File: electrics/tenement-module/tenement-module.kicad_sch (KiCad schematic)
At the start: 28 parts, among them J1 WMBus, J2 South, J3 West, J4 East, U1 BA033CC0FP-E2, U2 MCP23009-E_SS, U3 WIRL-WMB8, U4 MAX3486

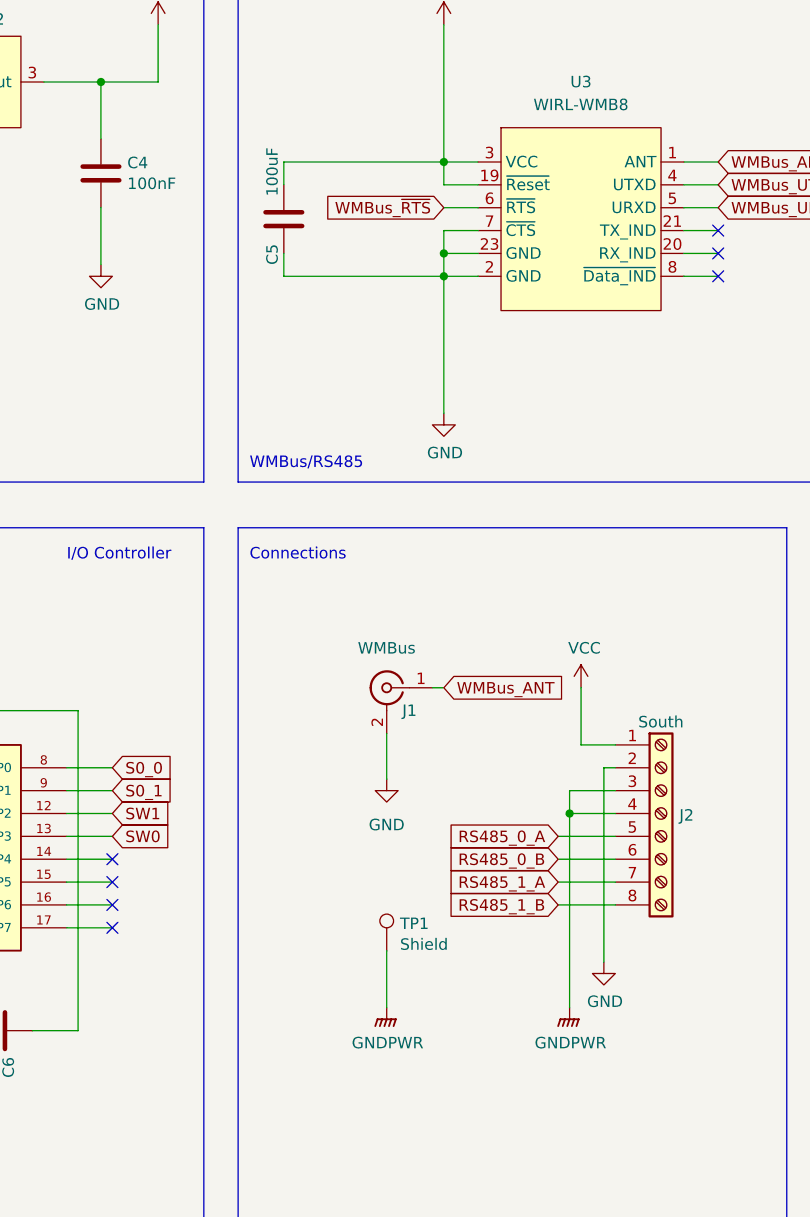
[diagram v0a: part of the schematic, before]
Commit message: Added product numbers for cost calculation
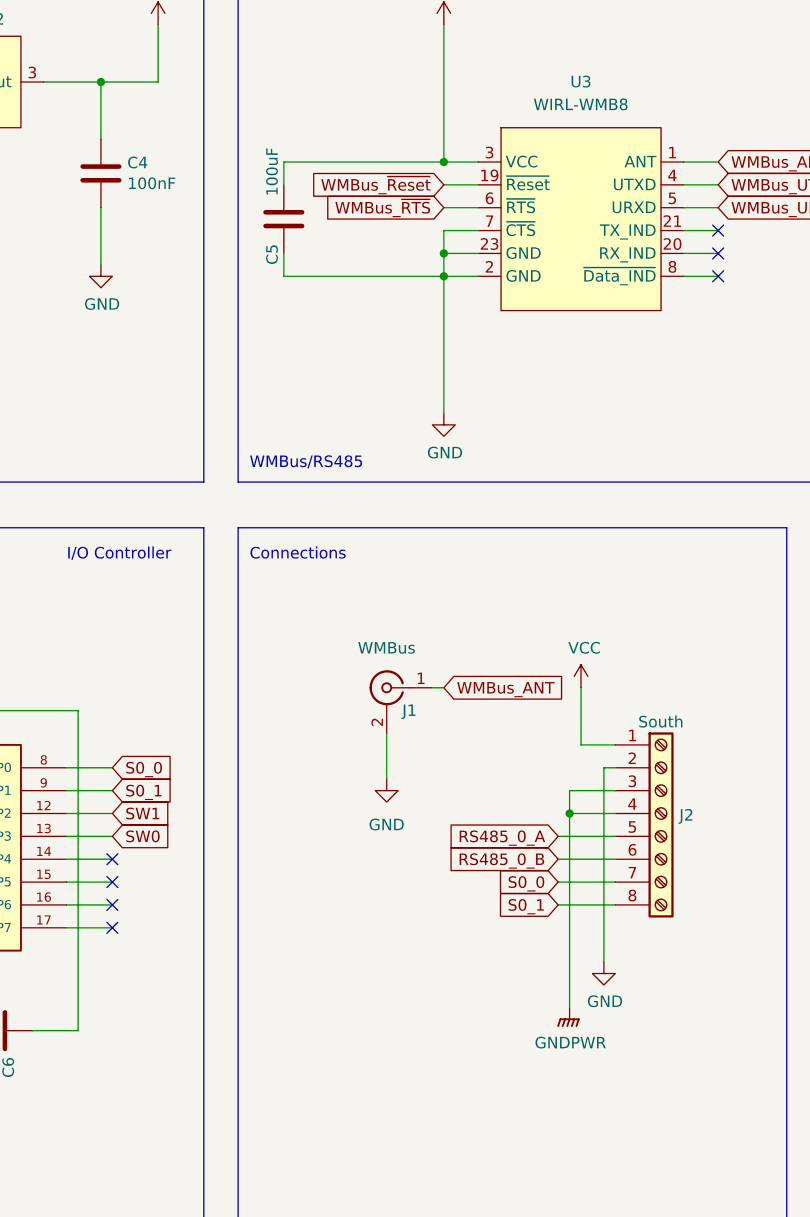
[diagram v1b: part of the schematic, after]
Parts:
- removed TP1: Shield, TestPoint:TestPoint_Pad_D4.0mm, symbol Connector:TestPoint
- J1: footprint (none) -> footprints:IPEX_20279-001E-01
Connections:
- net RS485_1_A is gone; now on net S0_0: J2.7 (Pin_7)
- net RS485_1_B is gone; now on net S0_1: J2.8 (Pin_8)
- net +3V3: no longer U3.19 (~{Reset})
- new net WMBus_~{Reset}: U3.19 (~{Reset})
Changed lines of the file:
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@@
   (junction (at 153.67 53.34) (diameter 0) (color 0 0 0 0)
   )
+  (junction (at 153.67 43.18) (diameter 0) (color 0 0 0 0)
+  )
   (junction (at 44.45 147.32) (diameter 0) (color 0 0 0 0)
   )
@@
   )
   (junction (at 153.67 55.88) (diameter 0) (color 0 0 0 0)
-  )
-  (junction (at 153.67 43.18) (diameter 0) (color 0 0 0 0)
   )
   (no_connect (at 184.15 55.88))
@@
   (no_connect (at 215.9 120.65))
   (no_connect (at 251.46 113.03))
-  (wire (pts (xy 147.32 130.81) (xy 147.32 137.16))
-    (stroke (width 0) (type default) (color 0 0 0 0))
-  )
   (polyline (pts (xy 130.81 78.74) (xy 130.81 20.32))
     (stroke (width 0) (type default) (color 0 0 0 0))
@@
     (stroke (width 0) (type default) (color 0 0 0 0))
   )
-  (wire (pts (xy 153.67 45.72) (xy 153.67 43.18))
-    (stroke (width 0) (type default) (color 0 0 0 0))
-  )
   (wire (pts (xy 157.48 53.34) (xy 153.67 53.34))
     (stroke (width 0) (type default) (color 0 0 0 0))
@@
     (stroke (width 0) (type default) (color 0 0 0 0))
   )
+  (wire (pts (xy 153.67 45.72) (xy 157.48 45.72))
+    (stroke (width 0) (type default) (color 0 0 0 0))
+  )
   (wire (pts (xy 153.67 55.88) (xy 157.48 55.88))
     (stroke (width 0) (type default) (color 0 0 0 0))
   )
-  (wire (pts (xy 157.48 45.72) (xy 153.67 45.72))
-    (stroke (width 0) (type default) (color 0 0 0 0))
-  )
   (wire (pts (xy 31.75 156.21) (xy 31.75 157.48))
     (stroke (width 0) (type default) (color 0 0 0 0))
@@
     (stroke (width 0) (type default) (color 0 0 0 0))
   )
+  (wire (pts (xy 153.67 43.18) (xy 157.48 43.18))
+    (stroke (width 0) (type default) (color 0 0 0 0))
+  )
   (wire (pts (xy 172.72 120.65) (xy 166.37 120.65))
     (stroke (width 0) (type default) (color 0 0 0 0))
@@
   )
   (wire (pts (xy 215.9 125.73) (xy 222.25 125.73))
-    (stroke (width 0) (type default) (color 0 0 0 0))
-  )
-  (wire (pts (xy 153.67 43.18) (xy 157.48 43.18))
     (stroke (width 0) (type default) (color 0 0 0 0))
   )
@@
     )
   )
+  (global_label "WMBus_~{Reset}" (shape input) (at 153.67 45.72 180) (fields_autoplaced)
+    (effects (font (size 1.27 1.27)) (justify right))
+    (property "Intersheet References" "${INTERSHEET_REFS}" (id 0) (at 138.8272 45.6406 0)
+      (effects (font (size 1.27 1.27)) (justify right) hide)
+    )
+  )
   (global_label "WMBus_UTXD" (shape input) (at 184.15 45.72 0) (fields_autoplaced)
     (effects (font (size 1.27 1.27)) (justify left))
@@
     )
   )
+  (global_label "S0_1" (shape input) (at 166.37 125.73 180) (fields_autoplaced)
+    (effects (font (size 1.27 1.27)) (justify right))
+    (property "Intersheet References" "${INTERSHEET_REFS}" (id 0) (at 279.4 259.08 0)
+      (effects (font (size 1.27 1.27)) hide)
+    )
+  )
   (global_label "WMBus_URXD" (shape input) (at 215.9 118.11 180) (fields_autoplaced)
     (effects (font (size 1.27 1.27)) (justify right))
@@
     (effects (font (size 1.27 1.27)) (justify right))
     (property "Intersheet References" "${INTERSHEET_REFS}" (id 0) (at 0 0 0)
+      (effects (font (size 1.27 1.27)) hide)
+    )
+  )
+  (global_label "S0_0" (shape input) (at 166.37 123.19 180) (fields_autoplaced)
+    (effects (font (size 1.27 1.27)) (justify right))
+    (property "Intersheet References" "${INTERSHEET_REFS}" (id 0) (at 279.4 210.82 0)
       (effects (font (size 1.27 1.27)) hide)
     )
@@
     )
   )
-  (global_label "RS485_1_A" (shape input) (at 166.37 123.19 180) (fields_autoplaced)
-    (effects (font (size 1.27 1.27)) (justify right))
-    (property "Intersheet References" "${INTERSHEET_REFS}" (id 0) (at -8.89 8.89 0)
-      (effects (font (size 1.27 1.27)) hide)
-    )
-  )
   (global_label "I2C_SDA" (shape input) (at 251.46 118.11 180) (fields_autoplaced)
     (effects (font (size 1.27 1.27)) (justify right))
@@
   )
   (global_label "RS485_0_A" (shape input) (at 166.37 118.11 180) (fields_autoplaced)
-    (effects (font (size 1.27 1.27)) (justify right))
-    (property "Intersheet References" "${INTERSHEET_REFS}" (id 0) (at -8.89 8.89 0)
-      (effects (font (size 1.27 1.27)) hide)
-    )
-  )
-  (global_label "RS485_1_B" (shape input) (at 166.37 125.73 180) (fields_autoplaced)
     (effects (font (size 1.27 1.27)) (justify right))
     (property "Intersheet References" "${INTERSHEET_REFS}" (id 0) (at -8.89 8.89 0)
@@
     (pin "1")
     (pin "2")
-  )
-  (symbol (lib_id "Connector:TestPoint") (at 147.32 130.81 0) (unit 1)
-    (in_bom yes) (on_board yes)
-    (property "Reference" "TP1" (id 0) (at 148.7932 127.8128 0)
-      (effects (font (size 1.27 1.27)) (justify left))
-    )
-    (property "Value" "Shield" (id 1) (at 148.7932 130.1242 0)
-      (effects (font (size 1.27 1.27)) (justify left))
-    )
-    (property "Footprint" "TestPoint:TestPoint_Pad_D4.0mm" (id 2) (at 152.4 130.81 0)
-      (effects (font (size 1.27 1.27)) hide)
-    )
-    (property "Datasheet" "~" (id 3) (at 152.4 130.81 0)
-      (effects (font (size 1.27 1.27)) hide)
-    )
-    (pin "1")
-  )
-  (symbol (lib_id "power:GNDPWR") (at 147.32 137.16 0) (unit 1)
-    (in_bom yes) (on_board yes)
-    (property "Reference" "#PWR013" (id 0) (at 147.32 142.24 0)
-      (effects (font (size 1.27 1.27)) hide)
-    )
-    (property "Value" "GNDPWR" (id 1) (at 147.4216 141.0716 0))
-    (property "Footprint" "" (id 2) (at 147.32 138.43 0)
-      (effects (font (size 1.27 1.27)) hide)
-    )
-    (property "Datasheet" "" (id 3) (at 147.32 138.43 0)
-      (effects (font (size 1.27 1.27)) hide)
-    )
-    (pin "1")
   )
   (symbol (lib_id "Device:C") (at 31.75 106.68 0) (unit 1)
@@
     (property "Reference" "J1" (id 0) (at 149.86 104.14 0))
     (property "Value" "WMBus" (id 1) (at 147.32 97.2058 0))
-    (property "Footprint" "" (id 2) (at 147.32 101.6 0)
+    (property "Footprint" "footprints:IPEX_20279-001E-01" (id 2) (at 147.32 101.6 0)
       (effects (font (size 1.27 1.27)) hide)
     )
@@
       (reference "#PWR012") (unit 1) (value "GND") (footprint "")
     )
-    (path "/00000000-0000-0000-0000-000061bc8379"
-      (reference "#PWR013") (unit 1) (value "GNDPWR") (footprint "")
-    )
     (path "/00000000-0000-0000-0000-000061f36d22"
       (reference "#PWR014") (unit 1) (value "+3V3") (footprint "")
@@
     )
     (path "/69548258-90c8-452d-addd-b0df8984309b"
-      (reference "J1") (unit 1) (value "WMBus") (footprint "")
+      (reference "J1") (unit 1) (value "WMBus") (footprint "footprints:IPEX_20279-001E-01")
     )
     (path "/00000000-0000-0000-0000-000061a443ad"
@@
       (reference "R5") (unit 1) (value "10k") (footprint "Resistor_SMD:R_1206_3216Metric_Pad1.30x1.75mm_HandSolder")
     )
-    (path "/00000000-0000-0000-0000-000061bc6d73"
-      (reference "TP1") (unit 1) (value "Shield") (footprint "TestPoint:TestPoint_Pad_D4.0mm")
-    )
     (path "/00000000-0000-0000-0000-00006192f73f"

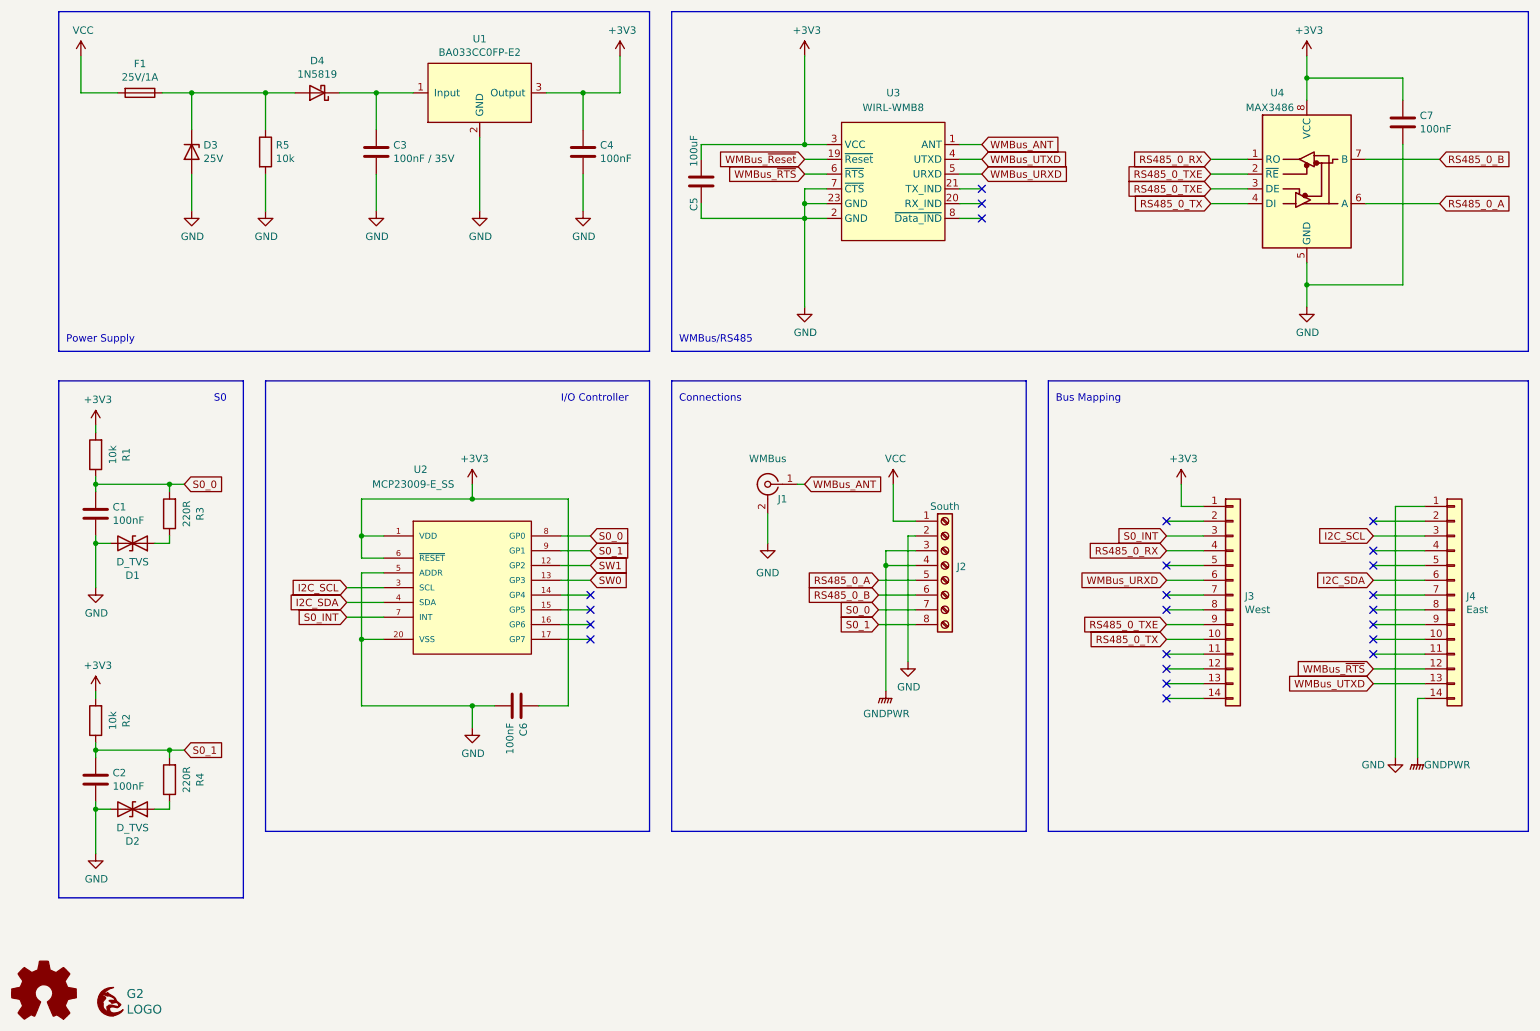
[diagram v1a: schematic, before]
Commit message: INOA-372 Fix out of stock components in TM module
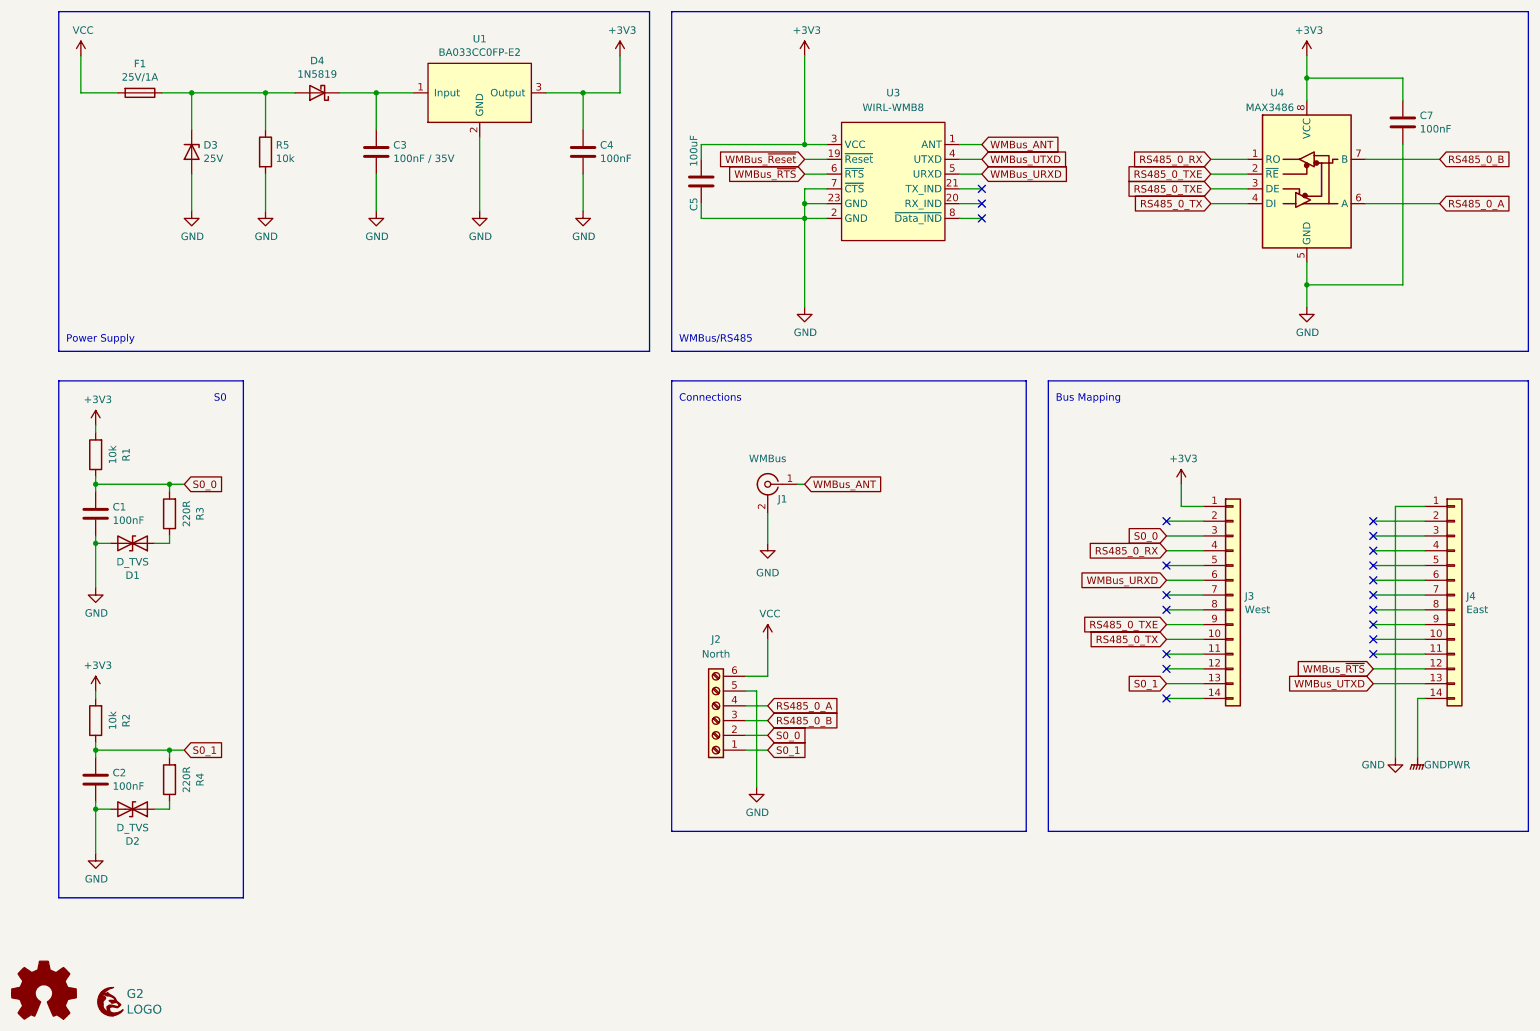
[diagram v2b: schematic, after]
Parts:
- removed C6: 100nF, Capacitor_SMD:C_1206_3216Metric_Pad1.33x1.80mm_HandSolder, symbol Device:C
- removed J2: South, footprints:PHOENIX_1727078, symbol Connector:Screw_Terminal_01x08
- removed U2: MCP23009-E_SS, SOP65P780X200-20N, symbol MCP23009-E_SS:MCP23009-E_SS
- added J2: North, footprints:PHOENIX_1935200, symbol Connector:Screw_Terminal_01x06
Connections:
- net S0_INT is gone; now on net S0_0: J3.3 (Pin_3)
- net GND: now also J2.5 (Pin_5)
- net RS485_0_A: now also J2.4 (Pin_4)
- net RS485_0_B: now also J2.3 (Pin_3)
- net S0_0: now also J2.2 (Pin_2)
- net S0_1: now also J3.13 (Pin_13), J2.1 (Pin_1)
- net VCC: now also J2.6 (Pin_6)
- net I2C_SCL: no longer names the net of J4.3 (Pin_3)
- net I2C_SDA: no longer names the net of J4.6 (Pin_6)
- no-connect marks 23 -> 20
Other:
- note removed: "I/O Controller"
